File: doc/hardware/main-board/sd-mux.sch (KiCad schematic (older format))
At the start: 48 parts, among them J1 USDCARD, P1 USB_OTG, P10 MKDS 1,5/3, P2 629105136821, P3 61400416021, P4 61400416021, P5 IDC_02X04, P6 IDC_02X04, P7 MKDS 1,5/3, P8 CONN_02X02, P9 CONN_02X02, Q1 IRF7606PBF, Q2 IRF7606PBF, Q3 IRF7606PBF, Q4 IRF7606PBF, Q5 2N7002, Q6 2N7002, Q7 IRF7606PBF, Q8 IRF7606PBF, U1 TS3USB30EDGSR, U2 FT245RL, U3 74AHC1G14, U4 TS3A27518E, U5 74AHC1G14

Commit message: Replace Micro SD card with SD card socket.  Add fiducials
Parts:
- J1: value USDCARD -> SDCARD; footprint footprints:microsd_socket -> EAGLE-INPUT_OUTPUT_CONNECTORS-rev17c:693063020911; symbol USDCARD -> SDCARD; mfrn# (none) -> 693063020911
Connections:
- net labels added: CLK, CMD, DAT0, DAT1, DAT2, DAT3
- wire segments 285 -> 291

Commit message: Refactor relay section so that it obeys mains isolation.  Delete headers, rearrange so that 'live' and 'neutral' sections are separated.  Rejig pinout so that unused pins never become live, and rotate terminals so that they can be accesed from the end of the board.
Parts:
- removed P8, P9: CONN_02X02, footprints:PSB_IDC_4x2, symbol CONN_02X02
- added FID1, FID2, FID3, FID4: Fiducial, Fiducials:Fiducial_1mm_Dia_2.54mm_Outer_CopperTop, symbol Fiducial
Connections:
- net labels added: E, Lin, Lout, Nin, Nout
- wire segments 291 -> 285

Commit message: Move 8w headers up so can fit shrouded 10w versions, flip so can use right angled
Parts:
- removed P5, P6: IDC_02X04, footprints:PSB_IDC_4x2, symbol CONN_02X04
- added P5, P6: Conn_02x05_Odd_Even, symbol Connector_Generic:Conn_02x05_Odd_Even
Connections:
- wire segments 285 -> 360

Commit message: Fix up missing footprints, replace 8w IDC with 10w on PCB so can use common ribbon cables
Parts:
- P1, P2: symbol USB_OTG-RESCUE-sd-mux -> USB_OTG
- P3, P4: symbol USB_A-RESCUE-sd-mux -> USB_A
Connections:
- wire segments 360 -> 289

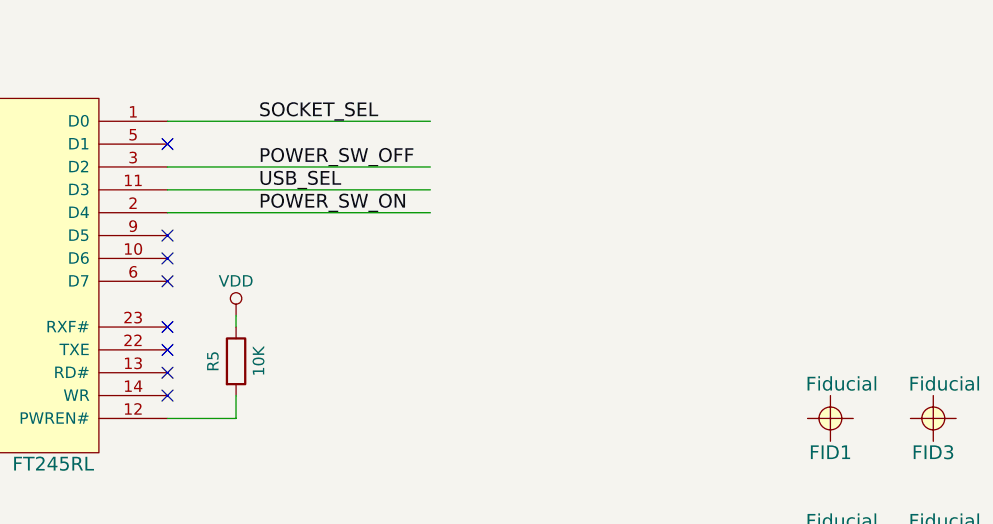
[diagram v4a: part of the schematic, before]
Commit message: Pin out spare GPIOs to a header, eg to match ebay '4 channel relay module Arduino RPi'
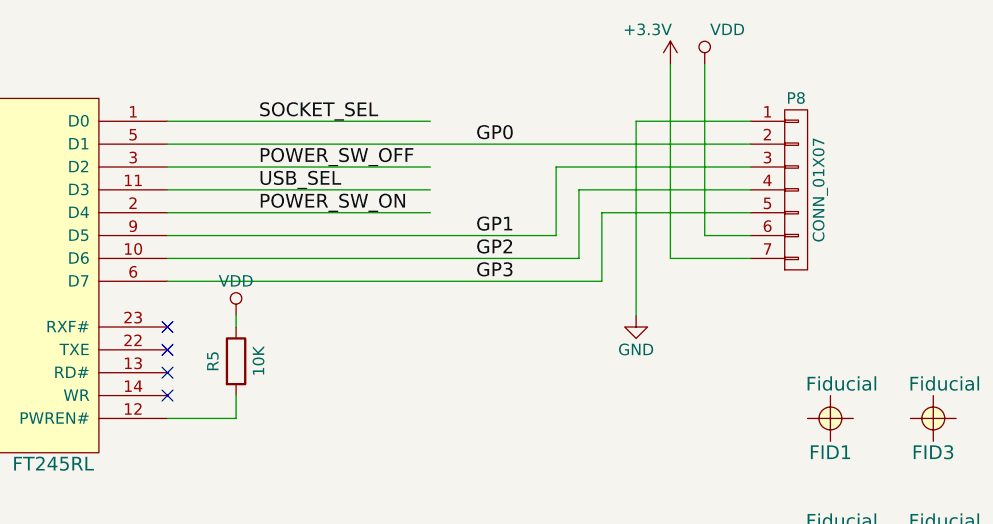
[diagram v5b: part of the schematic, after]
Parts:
- added P8: CONN_01X07, Connector_PinHeader_2.54mm:PinHeader_1x07_P2.54mm_Vertical, symbol CONN_01X07
- P5, P6: footprint (none) -> Connector_IDC:IDC-Header_2x05_P2.54mm_Vertical
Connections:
- net labels added: +3.3V, GP0, GP1, GP2, GP3
- wire segments 289 -> 305
- no-connect marks 15 -> 11
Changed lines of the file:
@@
 NoConn ~ 4100 2150
 NoConn ~ 4100 2050
-NoConn ~ 4100 1850
-NoConn ~ 4100 1750
-NoConn ~ 4100 1650
-NoConn ~ 4100 1250
 NoConn ~ 1150 1650
 $Comp
@@
 F 0 "P5" H 9500 5267 50  0000 C CNN
 F 1 "Conn_02x05_Odd_Even" H 9500 5176 50  0000 C CNN
-F 2 "" H 9450 4850 50  0001 C CNN
+F 2 "Connector_IDC:IDC-Header_2x05_P2.54mm_Vertical" H 9450 4850 50  0001 C CNN
 F 3 "~" H 9450 4850 50  0001 C CNN
 	1    9450 4850
@@
 F 0 "P6" H 9500 6217 50  0000 C CNN
 F 1 "Conn_02x05_Odd_Even" H 9500 6126 50  0000 C CNN
-F 2 "" H 9450 5800 50  0001 C CNN
+F 2 "Connector_IDC:IDC-Header_2x05_P2.54mm_Vertical" H 9450 5800 50  0001 C CNN
 F 3 "~" H 9450 5800 50  0001 C CNN
 	1    9450 5800
@@
 	9250 6150 9250 6000
 Connection ~ 9850 6150
+Wire Wire Line
+	4100 1650 5800 1650
+Wire Wire Line
+	5800 1650 5800 1350
+Wire Wire Line
+	5800 1350 6650 1350
+Wire Wire Line
+	4100 1750 5900 1750
+Wire Wire Line
+	5900 1750 5900 1450
+Wire Wire Line
+	5900 1450 6650 1450
+Wire Wire Line
+	4100 1850 6000 1850
+Wire Wire Line
+	6000 1850 6000 1550
+Wire Wire Line
+	6000 1550 6650 1550
+$Comp
+L CONN_01X07 P8
+U 1 1 5AFDF0B7
+P 6850 1450
+F 0 "P8" H 6850 1850 50  0000 C CNN
+F 1 "CONN_01X07" V 6950 1450 50  0000 C CNN
+F 2 "Connector_PinHeader_2.54mm:PinHeader_1x07_P2.54mm_Vertical" H 6850 1450 50  0001 C CNN
+F 3 "" H 6850 1450 50  0000 C CNN
+	1    6850 1450
+	1    0    0    -1
+$EndComp
+Wire Wire Line
+	6650 1650 6450 1650
+Wire Wire Line
+	6450 1650 6450 900
+Wire Wire Line
+	6650 1750 6300 1750
+Wire Wire Line
+	6300 1750 6300 900
+Wire Wire Line
+	6650 1150 6150 1150
+Wire Wire Line
+	6150 1150 6150 2000
+$Comp
+L GND #PWR045
+U 1 1 5AFDF763
+P 6150 2000
+F 0 "#PWR045" H 6150 1750 50  0001 C CNN
+F 1 "GND" H 6150 1850 50  0000 C CNN
+F 2 "" H 6150 2000 50  0000 C CNN
+F 3 "" H 6150 2000 50  0000 C CNN
+	1    6150 2000
+	1    0    0    -1
+$EndComp
+$Comp
+L VDD #PWR046
+U 1 1 5AFDF810
+P 6450 900
+F 0 "#PWR046" H 6450 750 50  0001 C CNN
+F 1 "VDD" H 6550 1050 50  0000 C CNN
+F 2 "" H 6450 900 50  0000 C CNN
+F 3 "" H 6450 900 50  0000 C CNN
+	1    6450 900
+	1    0    0    -1
+$EndComp
+$Comp
+L +3.3V #PWR047
+U 1 1 5AFDF8BD
+P 6300 900
+F 0 "#PWR047" H 6300 750 50  0001 C CNN
+F 1 "+3.3V" H 6200 1050 50  0000 C CNN
+F 2 "" H 6300 900 50  0000 C CNN
+F 3 "" H 6300 900 50  0000 C CNN
+	1    6300 900
+	1    0    0    -1
+$EndComp
+Wire Wire Line
+	4100 1250 6650 1250
+Text Label 5450 1250 0    60   ~ 0
+GP0
+Text Label 5450 1650 0    60   ~ 0
+GP1
+Text Label 5450 1750 0    60   ~ 0
+GP2
+Text Label 5450 1850 0    60   ~ 0
+GP3
 $EndSCHEMATC

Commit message: Label up inputs and add URL in silk
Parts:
- J1: value SDCARD -> 693063020911; mfr (none) -> Wurth
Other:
- note added: "GPIO"
- note added: "MicroUSB host\ncontrol port"
- note added: "SD card output DUT"
- note added: "SD card output TS"
- note added: "SD card socket"
- note added: "Switched MicroUSB host\n"
- note added: "Switched USB device DUT"
- note added: "Switched USB device TS"
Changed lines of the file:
@@
 P 14800 4600
 F 0 "J1" H 14650 5200 60  0000 C CNN
-F 1 "SDCARD" H 14800 4050 60  0000 C CNN
+F 1 "693063020911" H 14900 3900 60  0000 C CNN
 F 2 "EAGLE-INPUT_OUTPUT_CONNECTORS-rev17c:693063020911" H 14800 3900 60  0001 C CNN
 F 3 "" H 14800 4600 60  0000 C CNN
 F 4 "693063020911" H 14800 4600 60  0001 C CNN "mfrn#"
+F 5 "Wurth" H 14800 4600 60  0001 C CNN "mfr"
 	1    14800 4600
 	1    0    0    -1
@@
 Text Label 5450 1850 0    60   ~ 0
 GP3
+Text Notes 14550 3900 0    60   ~ 0
+SD card socket
+Text Notes 700  6050 0    60   ~ 0
+Switched MicroUSB host\n
+Text Notes 6000 6050 0    60   ~ 0
+Switched USB device DUT
+Text Notes 6450 8000 0    60   ~ 0
+Switched USB device TS
+Text Notes 9100 4350 0    60   ~ 0
+SD card output DUT
+Text Notes 9100 6550 0    60   ~ 0
+SD card output TS
+Text Notes 650  1150 0    60   ~ 0
+MicroUSB host\ncontrol port
+Text Notes 6750 2000 0    60   ~ 0
+GPIO
 $EndSCHEMATC
